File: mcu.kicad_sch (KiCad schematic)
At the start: 37 parts, among them IC1 ESDALC6V1W5, J10 STM32-Prog-Header, J8 OLED, J9 USB_C_Receptacle_USB2.0_16P, SW1 RESET, SW2 SW_SPDT, U12 8MHz, U13 STM32G491KEUx, U15 MCP2542FD-E/SN, U16 MCP9700AT-ETT, U17 MCP9700AT-ETT, U18 MCP9700AT-ETT

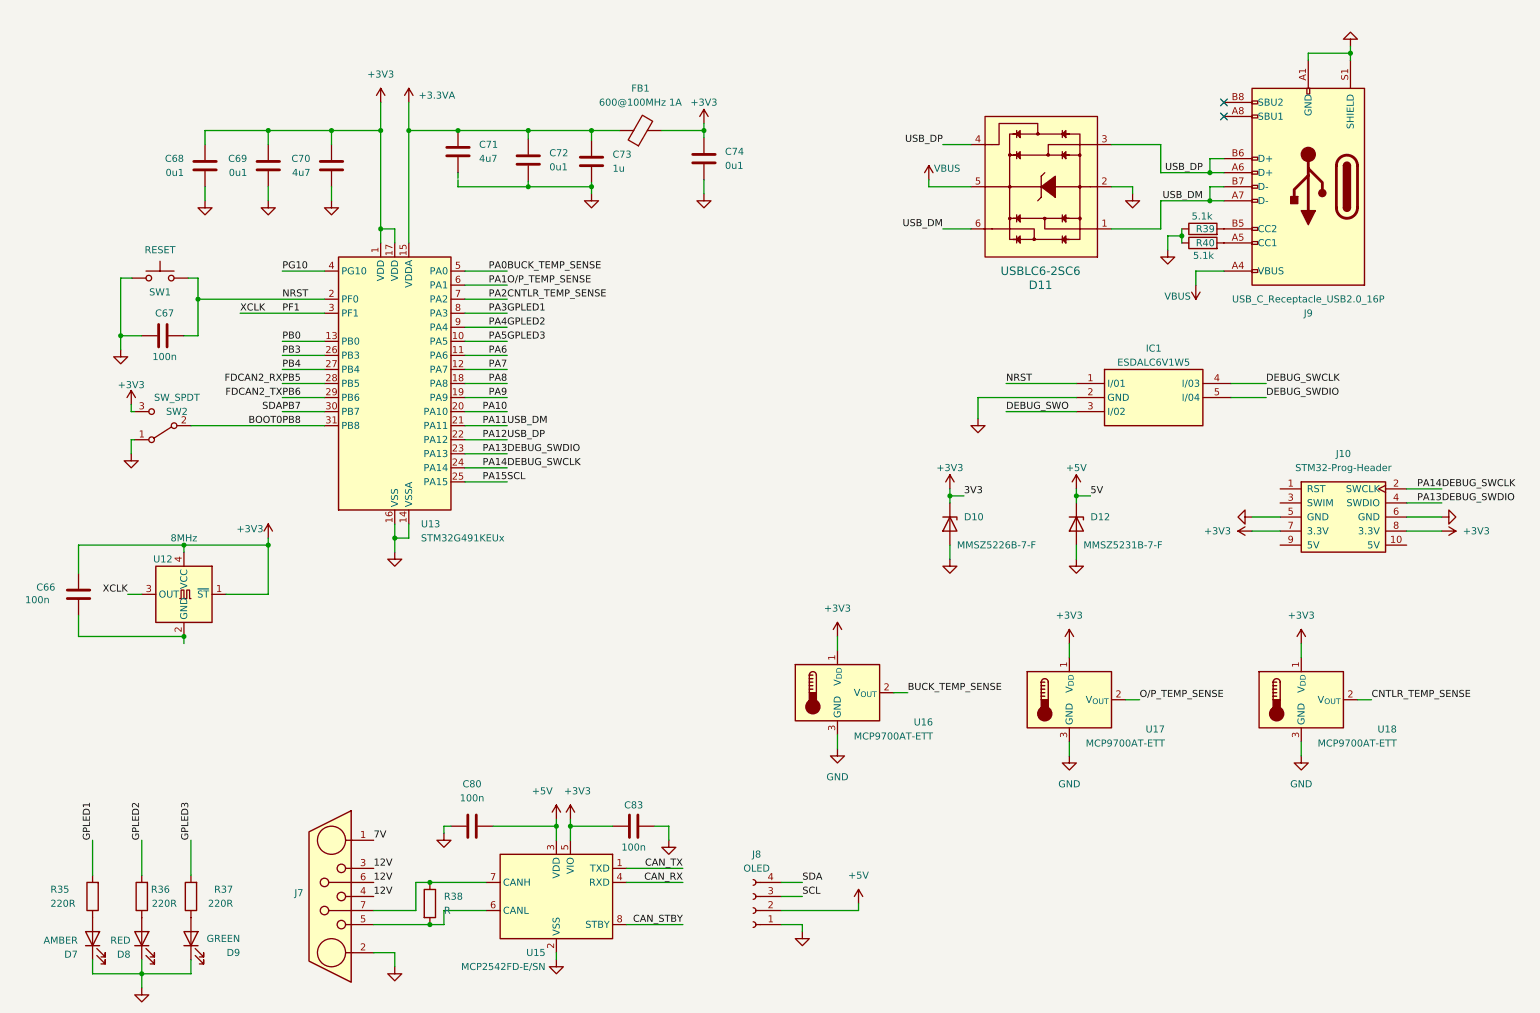
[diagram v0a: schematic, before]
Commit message: transferred correct schematics to rev2
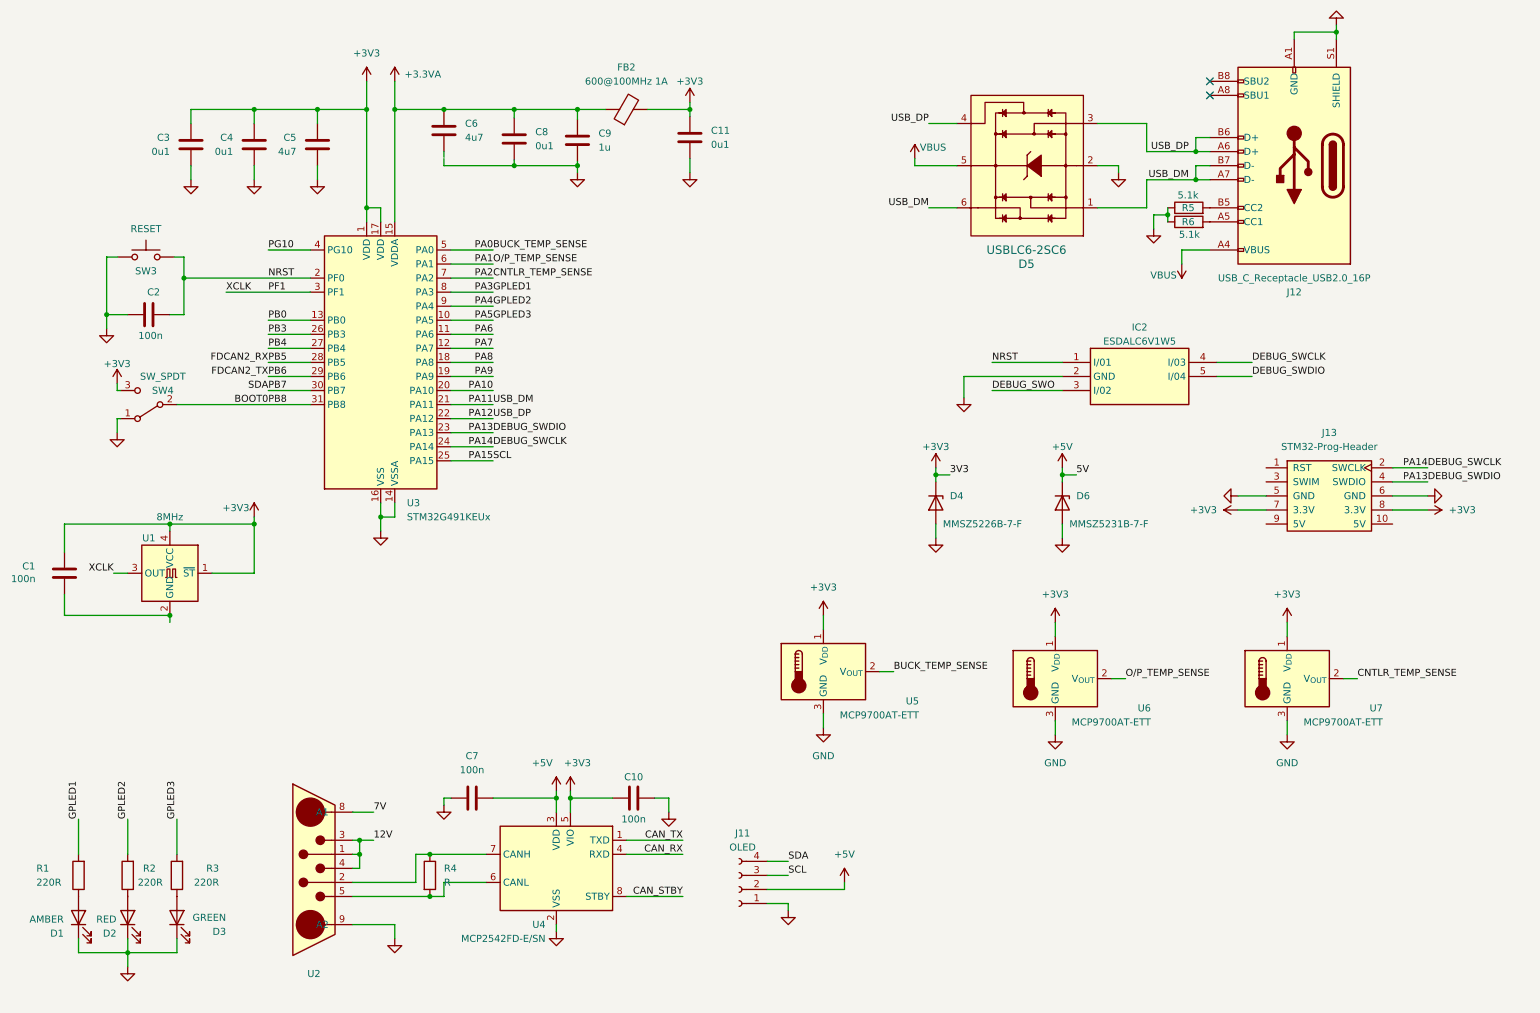
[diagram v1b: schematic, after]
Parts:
- removed C66, C67, C80, C83: 100n, Capacitor_SMD:C_0402_1005Metric, symbol Device:C
- removed C68, C69: 0u1, symbol Device:C
- removed C70: 4u7, symbol Device:C
- removed C71: 4u7, Capacitor_SMD:C_0603_1608Metric, symbol Device:C
- removed C72, C74: 0u1, Capacitor_SMD:C_0603_1608Metric, symbol Device:C
- removed C73: 1u, Capacitor_SMD:C_0603_1608Metric, symbol Device:C
- removed D10: MMSZ5226B-7-F, Diode_SMD:D_SOD-123, symbol Device:D_Zener
- removed D11: USBLC6-2SC6, BP_FTP:SOT23-6L_STM-L, symbol dk_TVS-Diodes:USBLC6-2SC6
- removed D12: MMSZ5231B-7-F, Diode_SMD:D_SOD-123, symbol Device:D_Zener
- removed D7: AMBER, LED_SMD:LED_0805_2012Metric, symbol Device:LED
- removed D8: RED, LED_SMD:LED_0805_2012Metric, symbol Device:LED
- removed D9: GREEN, LED_SMD:LED_0805_2012Metric, symbol Device:LED
- removed FB1: 600@100MHz 1A, Inductor_SMD:L_0603_1608Metric, symbol Device:FerriteBead
- removed IC1: ESDALC6V1W5, BP_FTP:SOT65P210X110-5N, symbol RF_Parts:ESDALC6V1W5
- removed J10: STM32-Prog-Header, ecocad_lib_footprints:IDC-STM32-Prog-Header_2x05_P2.54mm_Vertical, symbol ecocad_lib_symbols:STM32-Prog-Header
- removed J7: ~, ecocad:09692009032, symbol ecocad_lib_symbols:DB7W2
- removed J8: OLED, BP_FTP:Display_128x64_096_I2C, symbol Connector:Conn_01x04_Socket
- removed J9: USB_C_Receptacle_USB2.0_16P, symbol Connector:USB_C_Receptacle_USB2.0_16P
- removed R35, R36, R37: 220R, Resistor_SMD:R_0805_2012Metric, symbol Device:R
- removed R38: R, symbol Device:R
- removed R39, R40: 5.1k, Resistor_SMD:R_0805_2012Metric, symbol Device:R
- removed SW1: RESET, Button_Switch_THT:SW_PUSH_6mm_H5mm, symbol Switch:SW_Push
- removed SW2: SW_SPDT, Button_Switch_SMD:SW_SPDT_PCM12, symbol Switch:SW_SPDT
- removed U12: 8MHz, Crystal:Crystal_SMD_3225-4Pin_3.2x2.5mm, symbol RF_Parts:SG-3225CAN
- removed U13: STM32G491KEUx, Package_DFN_QFN:QFN-32-1EP_5x5mm_P0.5mm_EP3.45x3.45mm, symbol MCU_ST_STM32G4:STM32G491KEUx
- removed U15: MCP2542FD-E/SN, Package_SO:SOIC-8_3.9x4.9mm_P1.27mm, symbol Interface_CAN_LIN:MCP2542FDxMF
- removed U16, U17, U18: MCP9700AT-ETT, Package_TO_SOT_SMD:SOT-23, symbol Sensor_Temperature:MCP9700Ax-ETT
- added C1, C10, C2, C7: 100n, Capacitor_SMD:C_0603_1608Metric, symbol Device:C
- added C11, C3, C4, C8: 0u1, Capacitor_SMD:C_0603_1608Metric, symbol Device:C
- added C5, C6: 4u7, Capacitor_SMD:C_0603_1608Metric, symbol Device:C
- added C9: 1u, Capacitor_SMD:C_0603_1608Metric, symbol Device:C
- added D1: AMBER, LED_SMD:LED_0805_2012Metric, symbol Device:LED
- added D2: RED, LED_SMD:LED_0805_2012Metric, symbol Device:LED
- added D3: GREEN, LED_SMD:LED_0805_2012Metric, symbol Device:LED
- added D4: MMSZ5226B-7-F, Diode_SMD:D_SOD-123, symbol Device:D_Zener
- added D5: USBLC6-2SC6, BP_FTP:SOT23-6L_STM-L, symbol dk_TVS-Diodes:USBLC6-2SC6
- added D6: MMSZ5231B-7-F, Diode_SMD:D_SOD-123, symbol Device:D_Zener
- added FB2: 600@100MHz 1A, Inductor_SMD:L_0603_1608Metric, symbol Device:FerriteBead
- added IC2: ESDALC6V1W5, BP_FTP:SOT65P210X110-5N, symbol RF_Parts:ESDALC6V1W5
- added J11: OLED, BP_FTP:Display_128x64_096_I2C, symbol Connector:Conn_01x04_Socket
- added J12: USB_C_Receptacle_USB2.0_16P, Connector_USB:USB_C_Receptacle_GCT_USB4105-xx-A_16P_TopMnt_Horizontal, symbol Connector:USB_C_Receptacle_USB2.0_16P
- added J13: STM32-Prog-Header, ecocad_lib_footprints:IDC-STM32-Prog-Header_2x05_P2.54mm_Vertical, symbol ecocad_lib_symbols:STM32-Prog-Header
- added R1, R2, R3: 220R, Resistor_SMD:R_0805_2012Metric, symbol Device:R
- added R4: R, Resistor_SMD:R_0603_1608Metric, symbol Device:R
- added R5, R6: 5.1k, Resistor_SMD:R_0805_2012Metric, symbol Device:R
- added SW3: RESET, Button_Switch_THT:SW_PUSH_6mm_H5mm, symbol Switch:SW_Push
- added SW4: SW_SPDT, Button_Switch_SMD:SW_SPDT_PCM12, symbol Switch:SW_SPDT
- added U1: 8MHz, Crystal:Crystal_SMD_3225-4Pin_3.2x2.5mm, symbol RF_Parts:SG-3225CAN
- added U2: ~, symbol ecocad_lib_symbols:DB7W2-Male
- added U3: STM32G491KEUx, Package_DFN_QFN:QFN-32-1EP_5x5mm_P0.5mm_EP3.45x3.45mm, symbol MCU_ST_STM32G4:STM32G491KEUx
- added U4: MCP2542FD-E/SN, Package_SO:SOIC-8_3.9x4.9mm_P1.27mm, symbol Interface_CAN_LIN:MCP2542FDxMF
- added U5, U6, U7: MCP9700AT-ETT, Package_TO_SOT_SMD:SOT-23, symbol Sensor_Temperature:MCP9700Ax-ETT
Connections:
- net +3.3VA: now also C6.1, C8.1, C9.1, FB2.1, U3.15 (VDDA)
- net +3V3: now also C1.2, C10.2, C11.1, C3.1, C4.1, C5.1, D4.1 (K), FB2.2, J13.7 (3.3V), J13.8 (3.3V), SW4.3 (C), U1.1 (~{ST}), U1.4 (VCC), U3.1 (VDD), U3.17 (VDD), U4.5 (VIO), U5.1 (V_{DD}), U6.1 (V_{DD}), U7.1 (V_{DD})
- net +5V: now also C7.2, D6.1 (K), J11.2 (Pin_2), U4.3 (VDD)
- net 12V: now also U2.1, U2.3, U2.4
- net 7V: now also U2.8 (A1)
- net BOOT0: now also SW4.2 (B), U3.31 (PB8)
- net BUCK_TEMP_SENSE: now also U3.5 (PA0), U5.2 (V_{OUT})
- net CAN_RX: now also U4.4 (RXD)
- net CAN_STBY: now also U4.8 (STBY)
- net CAN_TX: now also U4.1 (TXD)
- net CNTLR_TEMP_SENSE: now also U3.7 (PA2), U7.2 (V_{OUT})
- net DEBUG_SWCLK: now also IC2.4 (I/03), J13.2 (SWCLK), U3.24 (PA14)
- net DEBUG_SWDIO: now also IC2.5 (I/04), J13.4 (SWDIO), U3.23 (PA13)
- net DEBUG_SWO: now also IC2.3 (I/02)
- net FDCAN2_RX: now also U3.28 (PB5)
- net FDCAN2_TX: now also U3.29 (PB6)
- net GND: now also C10.1, C11.2, C2.1, C7.1, C8.2, C9.2, D1.1 (K), D2.1 (K), D3.1 (K), D4.2 (A), D5.2, D6.2 (A), IC2.2 (GND), J11.1 (Pin_1), J12.A1 (GND), J12.A12 (GND), J12.B1 (GND), J12.B12 (GND), J12.S1 (SHIELD), R5.1, R6.1, SW3.1, SW4.1 (A), U2.9 (A2), U4.2 (VSS), U4.9 (VSS), U5.3 (GND), U6.3 (GND), U7.3 (GND)
- net GNDA: now also C3.2, C4.2, C5.2, J13.5 (GND), J13.6 (GND), U3.14 (VSSA), U3.16 (VSS), U3.32 (VSS), U3.33 (VSS)
- net GPLED1: now also R1.2, U3.8 (PA3)
- net GPLED2: now also R2.2, U3.9 (PA4)
- net GPLED3: now also R3.2, U3.10 (PA5)
- net NRST: now also C2.2, IC2.1 (I/01), SW3.2, U3.2 (PF0)
- net O/P_TEMP_SENSE: now also U3.6 (PA1), U6.2 (V_{OUT})
- net PA10: now also U3.20 (PA10)
- net PA11: now also D5.1, D5.6, J12.A7 (D-), J12.B7 (D-), U3.21 (PA11)
- net PA12: now also D5.3, D5.4, J12.A6 (D+), J12.B6 (D+), U3.22 (PA12)
- net PA15: now also J11.3 (Pin_3), U3.25 (PA15)
- net PA6: now also U3.11 (PA6)
- net PA7: now also U3.12 (PA7)
- net PA8: now also U3.18 (PA8)
- net PA9: now also U3.19 (PA9)
- net PB0: now also U3.13 (PB0)
- net PB3: now also U3.26 (PB3)
- net PB4: now also U3.27 (PB4)
- net PB7: now also J11.4 (Pin_4), U3.30 (PB7)
- net PF1: now also U1.3 (OUT), U3.3 (PF1)
- net PG10: now also U3.4 (PG10)
- net VBUS: now also D5.5, J12.A4 (VBUS), J12.A9 (VBUS), J12.B4 (VBUS), J12.B9 (VBUS)
- new net: D1.2 (A), R1.1
- new net: R4.1, U2.2, U4.7 (CANH)
- new net: R4.2, U2.5, U4.6 (CANL)
- new net: J12.A5 (CC1), R6.2
- new net: J12.B5 (CC2), R5.2
- new net: D3.2 (A), R3.1
- new net: C1.1, U1.2 (GND)
- new net: D2.2 (A), R2.1

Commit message: Fixed missing symbols and 7V sensor labels
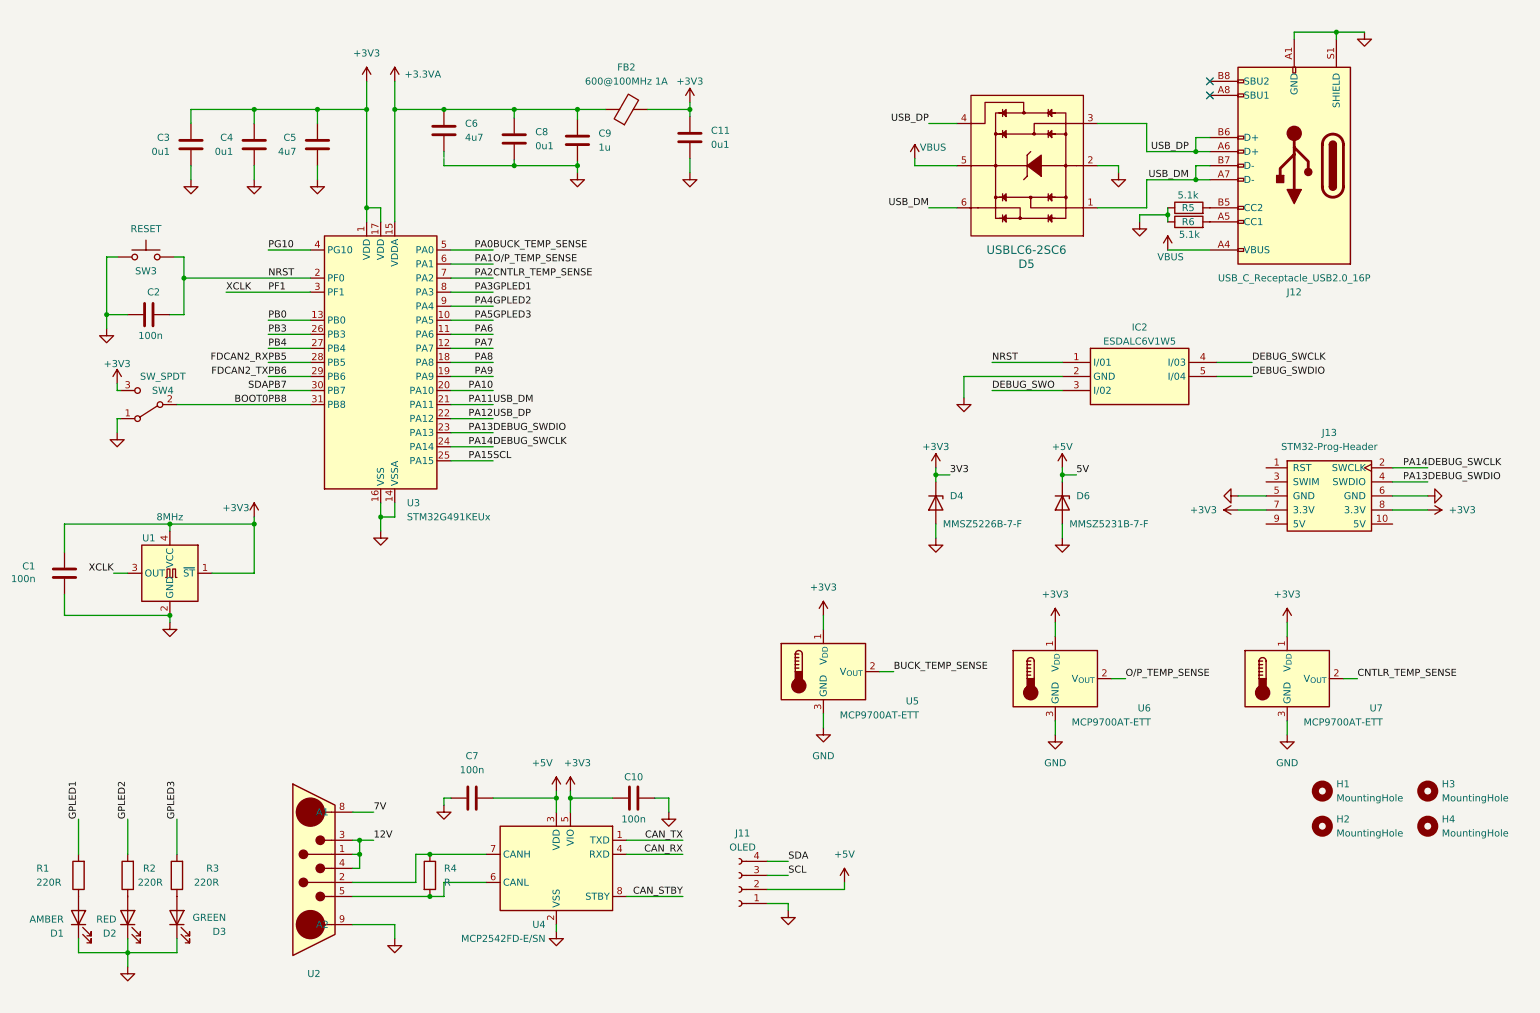
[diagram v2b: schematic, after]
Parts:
- added H1, H2, H3, H4: MountingHole, MountingHole:MountingHole_3.5mm, symbol Mechanical:MountingHole
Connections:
- net GNDA: now also C1.1, U1.2 (GND)

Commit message: Added missing symbols
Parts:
- IC2: footprint BP_FTP:SOT65P210X110-5N -> ecocad_lib_footprints:SOT65P210X110-5N
- J11: footprint BP_FTP:Display_128x64_096_I2C -> ecocad_lib_footprints:Display_128x64_096_I2C
- U2: footprint (none) -> ecocad_lib_footprints:DB7W2-Male
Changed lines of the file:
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@@
 			)
 		)
-		(property "Footprint" "BP_FTP:SOT65P210X110-5N"
+		(property "Footprint" "ecocad_lib_footprints:SOT65P210X110-5N"
 			(at 227.33 173.66 0)
 			(effects
@@
 			)
 		)
-		(property "Footprint" "BP_FTP:Display_128x64_096_I2C"
+		(property "Footprint" "ecocad_lib_footprints:Display_128x64_096_I2C"
 			(at 144.78 173.99 0)
 			(effects
@@
 			)
 		)
-		(property "Footprint" ""
+		(property "Footprint" "ecocad_lib_footprints:DB7W2-Male"
 			(at 67.31 170.18 0)
 			(effects

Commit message: fixed footprints
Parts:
- D5: footprint BP_FTP:SOT23-6L_STM-L -> Package_TO_SOT_SMD:TSOT-23-6_HandSoldering
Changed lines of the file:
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@@
 			)
 		)
-		(property "Footprint" "BP_FTP:SOT23-6L_STM-L"
+		(property "Footprint" "Package_TO_SOT_SMD:TSOT-23-6_HandSoldering"
 			(at 191.77 48.26 0)
 			(effects

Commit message: updates on pcb layout
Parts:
- U2: footprint ecocad_lib_footprints:DB7W2-Male -> ecocad_lib_footprints:DB7W2-30A
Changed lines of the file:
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@@
 			)
 		)
-		(property "Footprint" "ecocad_lib_footprints:DB7W2-Male"
+		(property "Footprint" "ecocad_lib_footprints:DB7W2-30A"
 			(at 67.31 170.18 0)
 			(effects

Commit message: Started Layout and cleaned up schematic
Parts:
- J3: renamed from J13; footprint ecocad_lib_footprints:IDC-STM32-Prog-Header_2x05_P2.54mm_Vertical -> Connector_PinHeader_2.54mm:PinHeader_2x05_P2.54mm_Vertical
- U7: renamed from U2; footprint ecocad_lib_footprints:DB7W2-30A -> ecocad_lib_footprints:DB7W2-Female
- renumbered C1 to C32, C2 to C33, C3 to C34, C4 to C35, C5 to C36, C6 to C37, C7 to C38, C8 to C39, C9 to C40, C10 to C41, C11 to C42, FB2 to FB1, IC2 to IC1, J11 to J1, J12 to J2, R1 to R16, R2 to R17, R3 to R18, R4 to R19, R5 to R20, R6 to R21, SW3 to SW1, SW4 to SW2, U5 to U10, U6 to U11, U7 to U12, U1 to U6, U3 to U8, U4 to U9

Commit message: A
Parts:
- removed U7: ~, ecocad_lib_footprints:DB7W2-Female, symbol ecocad_lib_symbols:DB7W2-Male
- added C51: 100n, Capacitor_SMD:C_0603_1608Metric, symbol Device:C
- added R41, R42: 10k, Resistor_SMD:R_0805_2012Metric, symbol Device:R
- added TP3: MCO, Connector_PinHeader_2.54mm:PinHeader_1x01_P2.54mm_Vertical, symbol Connector:TestPoint
- R4: renamed from R19; value R -> 120R
- renumbered C37 to C10, C38 to C11, C39 to C12, C40 to C13, C41 to C14, C42 to C15, C32 to C5, C33 to C6, C34 to C7, C35 to C8, C36 to C9, D1 to D3, D2 to D4, D3 to D5, D4 to D6, D5 to D7, D6 to D8, R16 to R1, R17 to R2, R18 to R3, R20 to R5, R21 to R6, U6 to U3, U8 to U5, U9 to U6, U10 to U7, U11 to U8, U12 to U9
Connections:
- net CAN_RX is gone; now on net FDCAN2_RX: U6.4 (RXD)
- net CAN_TX is gone; now on net FDCAN2_TX: U6.1 (TXD)
- net PA10 is gone; now on net GPLED2: U5.20 (PA10)
- net PA9 is gone; now on net GPLED1: U5.19 (PA9)
- net PG10 is gone; now on net NRST: U5.4 (PG10)
- net +3V3: now also C51.2
- net BOOT0: now also R42.1; no longer SW2.2 (B)
- net GND: now also C10.2
- net GNDA: now also C51.1
- net GPLED1: no longer U5.8 (PA3)
- net GPLED2: no longer U5.9 (PA4)
- net NRST: now also R41.1; no longer C6.2, SW1.2, U5.2 (PF0)
- net PA8: now also TP3.1
- net CANH: now reaches R4.1, U6.7 (CANH)
- net CANL: now reaches R4.2, U6.6 (CANL)
- net PA6 renamed IMON_{7V}
- net PA7 renamed VMON_{7V}
- net PB0 renamed IMON_{12V}
- net PB3 renamed PG_{7V}
- net PB4 renamed PG_{12V}
- net PF1 renamed VMON_{12V}
- net VMON_{12V}: no longer U3.3 (OUT)
- new net: C6.2, R41.2, SW1.2
- new net: R42.2, SW2.2 (B)
- new net IMON_{IN}: U5.9 (PA4)
- new net VMON_{IN}: U5.8 (PA3)
- new net XCLK: U3.3 (OUT), U5.2 (PF0)
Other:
- moved on the sheet: C13, C5, C6, SW1, SW2, U3

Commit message: A
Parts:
- added JP6: Jumper_2_Open, symbol Jumper:Jumper_2_Open
- C12, C15, C7, C8: value 0u1 -> 100n
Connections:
- net +5V: now also J3.10 (5V), J3.9 (5V), JP6.1 (A)
- net PA11: no longer D7.1, J2.A7 (D-), J2.B7 (D-)
- net PA12: no longer D7.3, J2.A6 (D+), J2.B6 (D+)
- net VBUS: now also JP6.2 (B)
- new net: D7.1, J2.A7 (D-), J2.B7 (D-)
- new net: D7.3, J2.A6 (D+), J2.B6 (D+)
- no-connect marks 2 -> 4
